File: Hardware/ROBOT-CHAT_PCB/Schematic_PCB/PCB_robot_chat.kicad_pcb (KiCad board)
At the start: 4 copper layers, 64.5 x 57 mm, 95 parts, among them J1 Conn_01x04, J201 Conn_ST_STDC14, J3 Conn_01x02, J4 Conn_01x02, J5 Conn_01x02, J501 Conn_01x04, J502 Conn_01x04, J503 Conn_01x04, J504 Conn_01x04, J6 Conn_01x02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

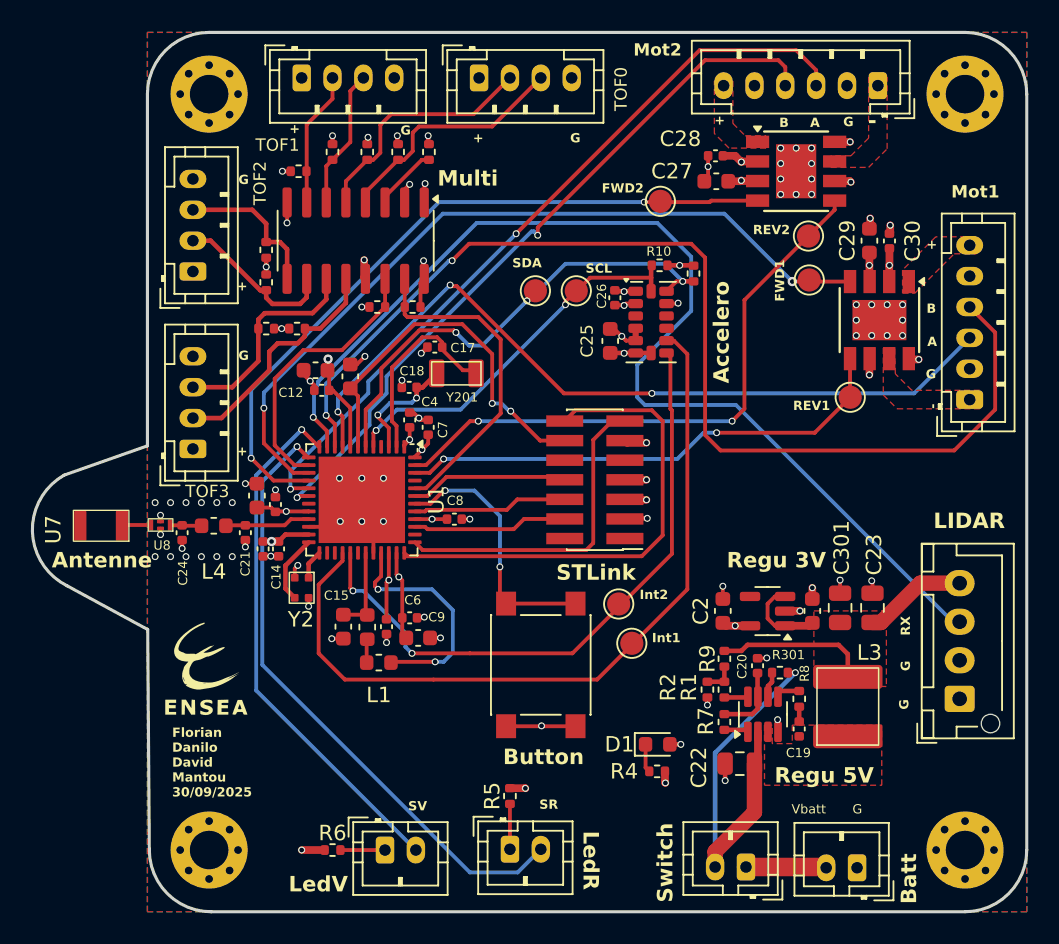
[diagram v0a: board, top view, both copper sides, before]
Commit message: Modif PCB after pin update, PCB version 5
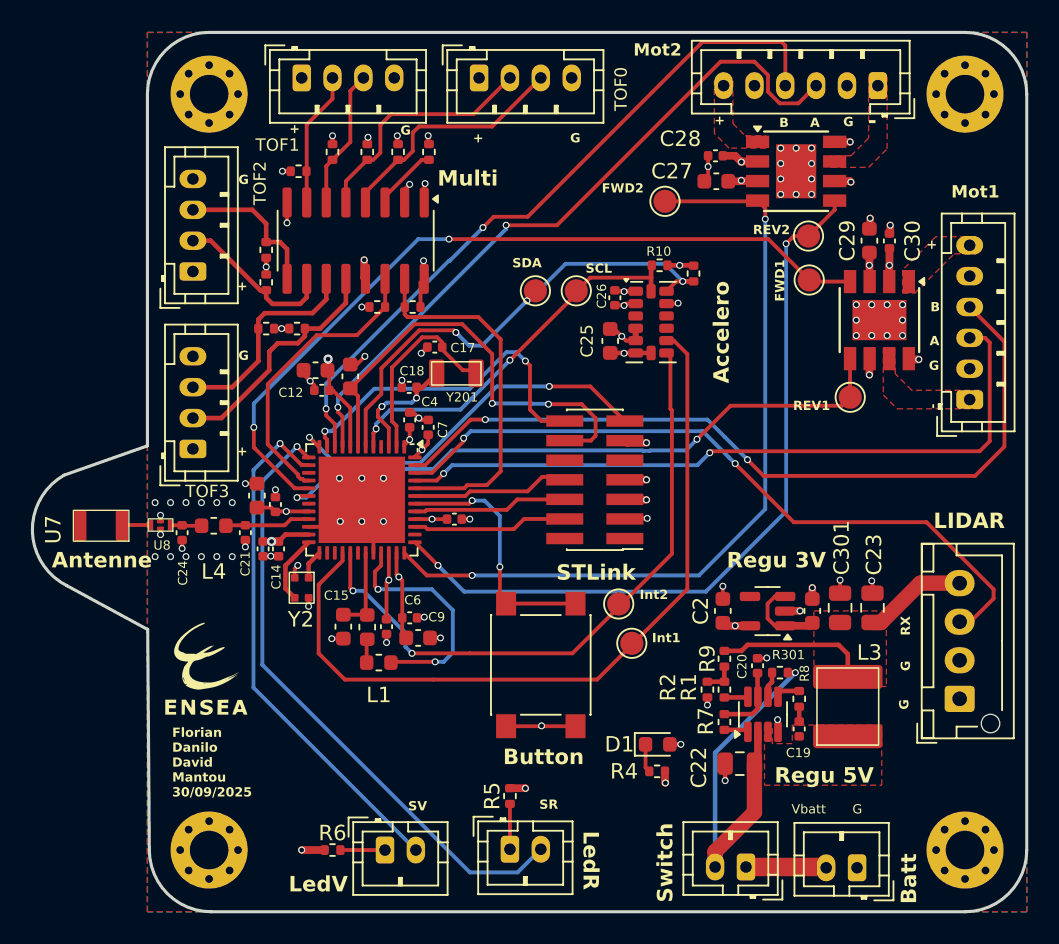
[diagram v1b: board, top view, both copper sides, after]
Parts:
- moved TP9 0.30 mm to (142.6, 40.0)
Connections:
- U1 pad 10: /Driver/Encodeur_1B -> /Driver/Encodeur_2B
- U1 pad 11: /STM/UART_TX -> /STM/VCP_TX
- U1 pad 12: /STM/STATUS_LEDV -> /STM/VCP_RX
- U1 pad 14: /Multiplexeur/SCL -> /STM/STATUS_LEDV
- U1 pad 15: /Driver/FWD_1 -> unconnected-(U1-PA6-Pad15)
- U1 pad 16: /Driver/FWD_2 -> /Multiplexeur/SCL
- U1 pad 17: /Driver/Encodeur_2A -> /Driver/FWD_1
- U1 pad 18: /Driver/Encodeur_2B -> /Driver/REV_1
- U1 pad 36: /STM/VCP_TX -> /Driver/FWD_2
- U1 pad 37: /STM/VCP_RX -> /Driver/REV_2
- U1 pad 45: unconnected-(U1-PB5-Pad45) -> /Driver/Encodeur_1A
- U1 pad 46: /Driver/REV_1 -> /STM/UART_TX
- U1 pad 47: /Driver/REV_2 -> /Driver/Encodeur_1B
- U1 pad 9: /Driver/Encodeur_1A -> /Driver/Encodeur_2A
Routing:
- net /STM/UART_TX: track 71.6 -> 46.4 mm, vias 1 -> 2
- net /Driver/Encodeur_1B: track 72.2 -> 51.7 mm
- net /Driver/REV_2: track 38.8 -> 49.6 mm
- net /STM/VCP_TX: track 31.7 -> 22.3 mm, vias 0 -> 2
- net /Driver/REV_1: track 32.8 -> 41.9 mm
- net /Driver/FWD_2: track 46.8 -> 52.5 mm
- net /Driver/Encodeur_1A: track 51.7 -> 46.1 mm, vias 3 -> 2
- net /STM/NRST: track 24.6 -> 29.3 mm
- net /Driver/Encodeur_2A: track 49.7 -> 45.7 mm
- net /STM/VCP_RX: track 21.2 -> 25.0 mm, vias 0 -> 2
- net /Multiplexeur/SDA: track 21.6 -> 23.8 mm
- net /Driver/Encodeur_2B: track 47.3 -> 46.0 mm
- net /Multiplexeur/SCL: track 18.0 -> 19.1 mm
- net /STM/STATUS_BUT: track 16.9 -> 16.4 mm
- net /STM/STATUS_LEDV: track 34.4 -> 33.9 mm
